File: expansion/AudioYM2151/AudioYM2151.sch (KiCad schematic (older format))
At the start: 10 parts, among them J1 D68K_64PIN_BOARD, J4 XilinxJTAG, U1 74LS125, U2 XC95144XL-TQ100

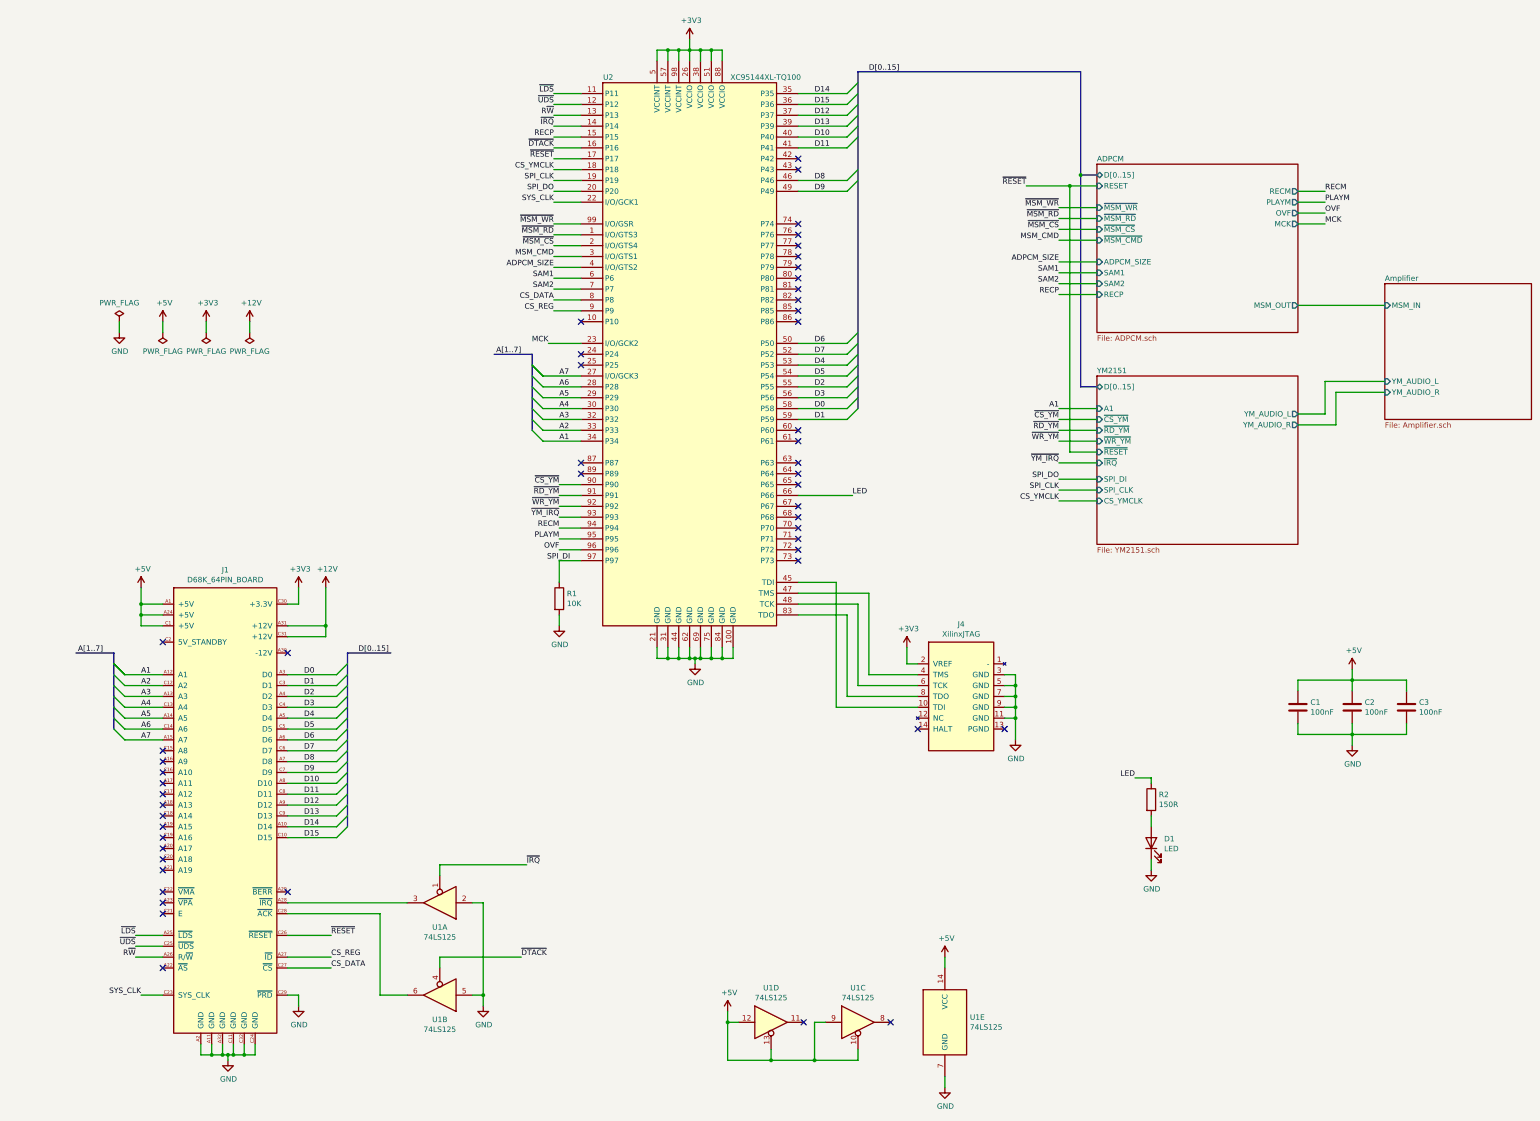
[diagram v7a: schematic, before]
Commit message: Removed MSM ADPCM chip from YM2151 board
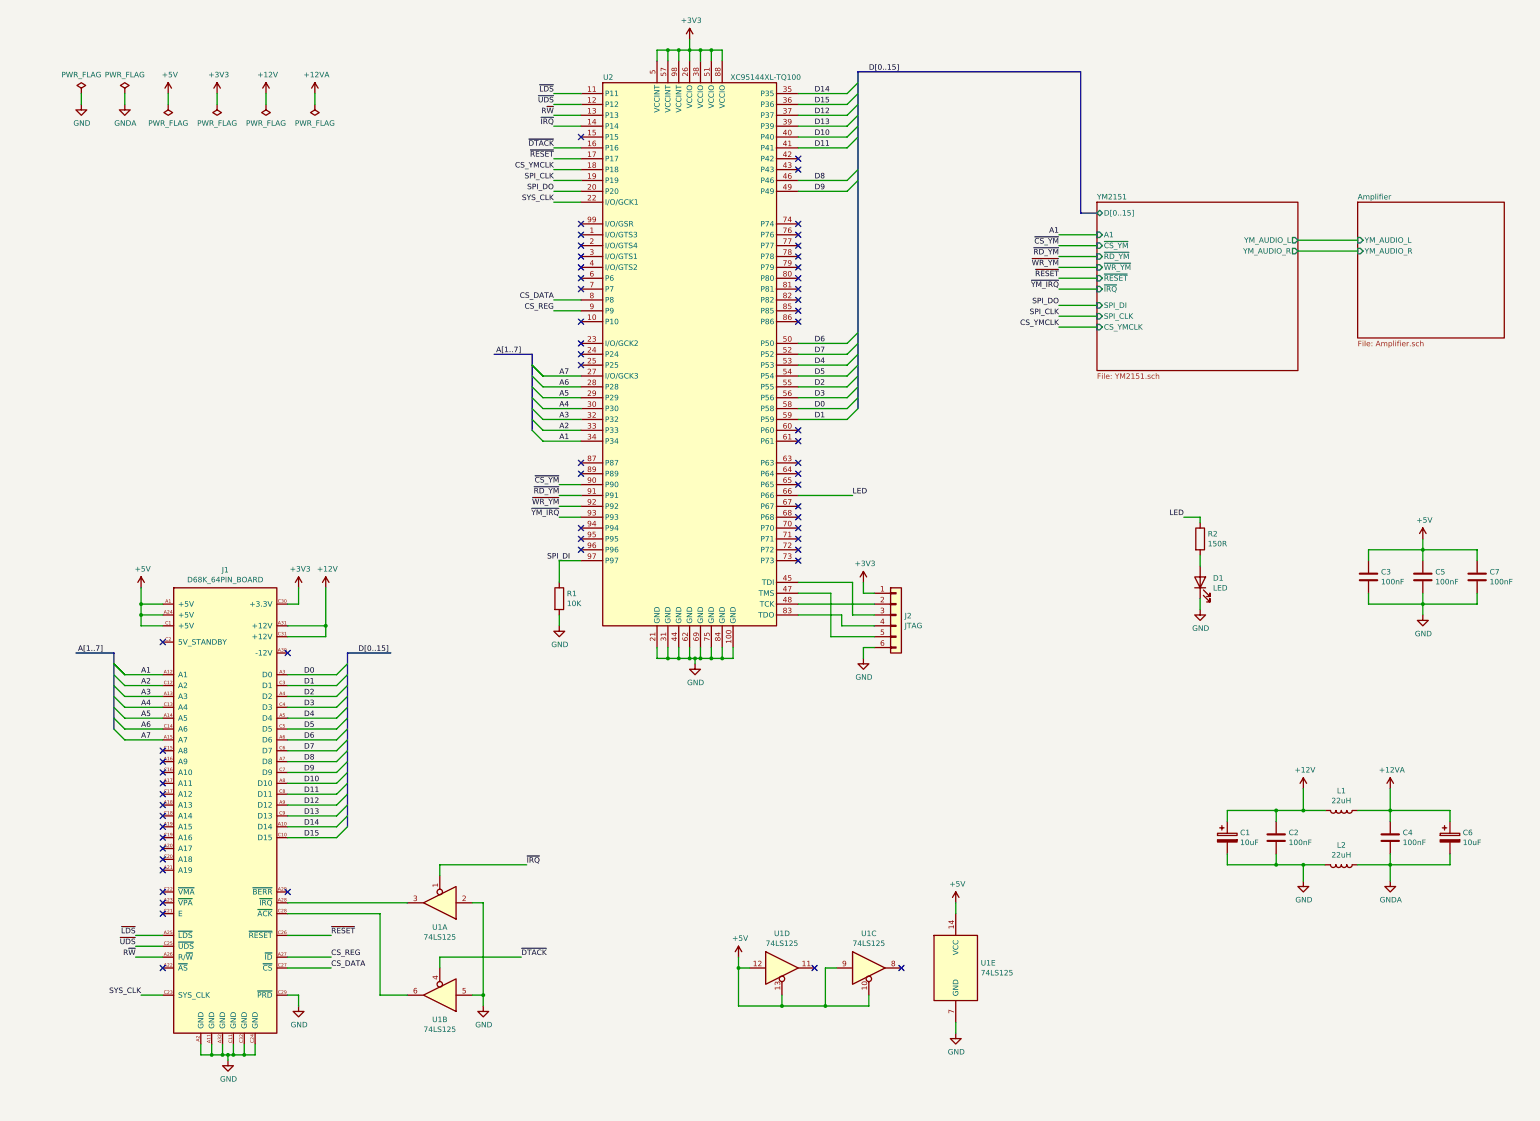
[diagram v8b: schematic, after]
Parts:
- removed J4: XilinxJTAG, Connector_IDC:IDC-Header_2x07_P2.54mm_Vertical, symbol Ddraig:XilinxJTAG
- added C1, C6: 10uF, Capacitor_THT:C_Disc_D5.0mm_W2.5mm_P2.50mm, symbol Device:CP
- added C2, C4: 100nF, Capacitor_THT:C_Disc_D5.0mm_W2.5mm_P2.50mm, symbol Device:C
- added J2: JTAG, Connector_PinHeader_2.54mm:PinHeader_1x06_P2.54mm_Vertical, symbol Connector_Generic:Conn_01x06
- added L1, L2: 22uH, Ferrite_THT:LairdTech_28C0236-0JW-10, symbol Device:L
- renumbered C1 to C3, C2 to C5, C3 to C7
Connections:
- net +12V: now also C1.1, C2.1, L1.2
- net +3V3: now also J2.1 (Pin_1)
- net GND: now also C1.2, C2.2, J2.6 (Pin_6), L2.2
- net at U2.45 (TDI): now also J2.3 (Pin_3)
- net at U2.47 (TMS): now also J2.5 (Pin_5)
- net at U2.48 (TCK): now also J2.2 (Pin_2)
- net at U2.83 (TDO): now also J2.4 (Pin_4)
- net ADPCM_SIZE: no longer names the net of U2.4 (I/O/GTS2)
- net MCK: no longer names the net of U2.23 (I/O/GCK2)
- net MSM_CMD: no longer names the net of U2.3 (I/O/GTS1)
- net OVF: no longer names the net of U2.96 (P96)
- net PLAYM: no longer names the net of U2.95 (P95)
- net RECM: no longer names the net of U2.94 (P94)
- net RECP: no longer names the net of U2.15 (P15)
- net SAM1: no longer names the net of U2.6 (P6)
- net SAM2: no longer names the net of U2.7 (P7)
- net ~MSM_CS: no longer names the net of U2.2 (I/O/GTS4)
- net ~MSM_RD: no longer names the net of U2.1 (I/O/GTS3)
- net ~MSM_WR: no longer names the net of U2.99 (I/O/GSR)
- new net +12VA: C4.1, C6.1, L1.1
- new net GNDA: C4.2, C6.2, L2.1
- no-connect marks 51 -> 61
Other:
- moved on the sheet: C3, C5, C7, D1, R2, U1C, U1D, U1E
